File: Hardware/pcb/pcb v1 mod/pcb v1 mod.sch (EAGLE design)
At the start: 48 parts, among them K1 JS-M1-9V-4, K2 JS-M1-9V-4, Q1 32.768kHz 12.5pF, Q10 MOSFET-NCHANNELBSS138, Q3 MOSFET-NCHANNELBSS138, Q4 MOSFET-NCHANNELBSS138, Q5 MOSFET-NCHANNELBSS138, Q6 MOSFET-NCHANNELBSS138, Q7 MOSFET-NCHANNELBSS138, Q8 MOSFET-NCHANNELBSS138, Q9 MOSFET-NCHANNELBSS138, U1 ADP3338AKCZ-3.3RL7

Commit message: Ruteo completo
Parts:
- removed D1, D2: 1N5819HW, diego:1N5819HW
- removed D3: (no value), SparkFun-LED:WS2812B
- removed G1: BATTERY-HOLDER_11.6MM, battery:BATTERY-HOLDER_11.6MM
- removed K1, K2: JS-M1-9V-4, relay:JS-M1-9V-4
- removed Q10, Q3, Q4, Q5, Q6, Q7, Q8, Q9: MOSFET-NCHANNELBSS138, SparkFun-DiscreteSemi:MOSFET-NCHANNELBSS138
- removed R14, R16: 100, rcl:R-US_R0805
- removed R15, R17: 1M, rcl:R-US_R0805
- removed R18, R19: 10k, rcl:R-US_R0805
- removed RFID1: GROVE-RFID, partes:GROVE-RFID
- removed U$1: DS1307SO8, SparkFun-FreqCtrl:DS1307SO8
- removed X1, X2: (no value), con-wago-500:W237-103
- added C10, C9: 100nF, rcl:C-USC0805
- added C8: 22pF, rcl:C-USC1206
- added J1: AVR_SPI_PRG_6PTH, SparkFun-Connectors:AVR_SPI_PRG_6PTH
- added JP2, JP4, JP5: (no value), SparkFun-Connectors:M041X04_NO_SILK
- added JP3, JP7: (no value), SparkFun-Connectors:M03PTH
- added JP8, JP9: M02PTH, SparkFun-Connectors:M02PTH
- added LED1: 5MMRGBLED, adafruit:5MMRGBLED
- added LVLSHF1: LEVELSHIFTER4, partes:LEVELSHIFTER4
- added R3, R4: 10k, rcl:R-US_R0805
- added U2: ATMEGA328P, SparkFun-DigitalIC:ATMEGA328_SMT
- added Y1: 16Mhz, SparkFun-FreqCtrl:CRYSTALHC49US
- C1, C2: value 1uF -> 10uF; device rcl:CPOL-US150CLZ-1010 -> rcl:CPOL-USE2.5-6
- C3: device rcl:C-USC0805 -> rcl:C-USC1206
- C4: value 1uF -> 100nF
- C7: value 100nF -> 22pF; device rcl:C-USC0805 -> rcl:C-USC1206
- Q1: value 32.768kHz 12.5pF -> 2N3906; device crystal:CRYSTALTC26H -> transistor-pnp:2N3906
- R10: value 100 -> 160R; device rcl:R-US_R0805 -> rcl:R-US_R1206
- R11: value 1M -> 100R
- R12: value 100 -> 100R
- R13: value 1M -> 100K
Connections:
- removed net LED: Q10.S, R19.1
- removed net N$13: Q6.G, R10.2
- removed net N$24: Q9.D, SG1.2
- removed net N$26: D3.DIN, Q10.D, R18.1
- removed net RFIDPW: R10.1, R11.2
- removed net RFIDTX33: Q5.S, R8.1
- removed net SCL33: Q3.S, R5.1
- removed net SDA33: Q4.S, R7.1
- new net AT_RST: J1.5, R13.2, U2.PC6(/RESET)
- new net ESP_RX_33: JP8.1, LVLSHF1.LV2
- new net ESP_TX_33: JP9.1, LVLSHF1.LV1
- new net LED_B: R12.1, U2.PD6(AIN0)
- new net LED_G: R11.1, U2.PB2(SS/OC1B)
- new net LED_R: R10.1, U2.PB1(OC1A)
- new net N$10: LED1.RED, R10.2
- new net N$8: JP9.2, MDL1.TXD
- new net RFID_PW: R1.1, U2.PD5(T1)
- new net RFID_TX: JP4.4, U2.PD2(INT0)
- new net SCL: JP5.3, R7.1, U2.PC5(ADC5/SCL)
- new net SDA: JP5.4, R6.1, U2.PC4(ADC4/SDA)
- net +3V3: now also C10.1, C3.1, C4.1, JP3.3, LVLSHF1.LV, MDL1.VCC, R4.2, R9.2; no longer C7.1, Q10.G, Q3.G, Q4.G, Q5.G, R19.2, R5.2, R7.2
- net +5V: now also C9.1, J1.2, JP2.4, JP5.2, LVLSHF1.HV, Q1.E, R13.1, R7.2, U2.AVCC, U2.VCC@1, U2.VCC@2; no longer C3.1, C4.1, C6.1, D1.C, D2.C, D3.VDD, K11.1, K21.1, R1.2, R18.2, R9.2, RFID1.VCC, SG1.1, U$1.VCC
- net BUZZER: now also SG1.1, U2.PC0(ADC0); no longer R16.1, R17.2
- net GND: now also C10.2, C8.2, C9.2, J1.6, JP2.1, JP3.1, JP4.1, JP5.1, JP7.2, LED1.GND, LVLSHF1.GND, MDL1.GND, R3.1, SG1.2, U2.AGND, U2.GND@1, U2.GND@2; no longer D3.VSS, G1.-, Q6.S, Q7.S, Q8.S, Q9.S, R11.1, R13.1, R15.1, R17.1, U$1.GND
- net N$11: now also C7.1, U2.PB6(XTAL1/TOSC1), Y1.1; no longer Q5.D, R9.1, RFID1.TX
- net N$12: now also C8.1, U2.PB7(XTAL2/TOSC2), Y1.2; no longer D1.A, K11.2, Q7.D
- net N$14: now also C6.1, U2.AREF; no longer Q7.G, R12.2
- net N$15: now also LED1.GREEN, R11.2; no longer K12.O, X1-3.KL
- net N$16: now also LED1.BLUE, R12.2; no longer K12.P, X1-2.KL
- net N$17: now also J1.3, U2.PB5(SCK); no longer K12.S, X1-1.KL
- net N$18: now also J1.1, U2.PB4(MISO); no longer D2.A, K21.2, Q8.D
- net N$19: now also J1.4, U2.PB3(MOSI/OC2); no longer Q8.G, R14.2
- net N$2: now also MDL1.CH_PD, R8.1; no longer Q1.2, U$1.X1
- net N$20: now also JP3.2, R5.2; no longer K22.O, X2-3.KL
- net N$21: now also LVLSHF1.HV1, U2.PD0(RXD); no longer K22.P, X2-2.KL
- net N$22: now also LVLSHF1.HV2, U2.PD1(TXD); no longer K22.S, X2-1.KL
- net N$23: now also JP4.2, Q1.C; no longer Q9.G, R16.2
- net N$3: now also MDL1.GPIO2, R4.1; no longer Q1.1, U$1.X2
- net N$4: now also MDL1.GPIO0, R5.1; no longer G1.+, U$1.VBATT
- net N$5: now also MDL1.GPIO15, R3.2; no longer Q3.D, R2.1, U$1.SCL
- net N$6: now also JP8.2, MDL1.RXD; no longer R1.1, U$1.SQW
- net N$7: now also Q1.B, R1.2, R2.1; no longer Q6.D, RFID1.GND
- net N$9: now also JP7.1, MDL1.REST, R9.1; no longer Q4.D, R6.1, U$1.SDA
- net RELE1: now also JP2.3, U2.PC1(ADC1); no longer R12.1, R13.2
- net RELE2: now also JP2.2, U2.PC2(ADC2); no longer R14.1, R15.2
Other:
- moved on the sheet: C1, C2, C3, C4, C5, C6, C7, JP1, MDL1, R1, R10, R11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

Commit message: Correcciones placa
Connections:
- net GND: now also JP1.2; no longer JP1.1
- net N$1: now also JP1.1; no longer JP1.2
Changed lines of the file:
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@@
 <wire x1="259.08" y1="27.94" x2="259.08" y2="20.32" width="0.1524" layer="91"/>
 <junction x="259.08" y="20.32"/>
-<pinref part="JP1" gate="G$1" pin="1"/>
-<wire x1="228.6" y1="30.48" x2="231.14" y2="30.48" width="0.1524" layer="91"/>
-<wire x1="231.14" y1="30.48" x2="231.14" y2="20.32" width="0.1524" layer="91"/>
+<wire x1="231.14" y1="33.02" x2="231.14" y2="20.32" width="0.1524" layer="91"/>
 <wire x1="231.14" y1="20.32" x2="251.46" y2="20.32" width="0.1524" layer="91"/>
 <junction x="251.46" y="20.32"/>
 <pinref part="C1" gate="G$1" pin="-"/>
+<pinref part="JP1" gate="G$1" pin="2"/>
+<wire x1="228.6" y1="33.02" x2="231.14" y2="33.02" width="0.1524" layer="91"/>
 </segment>
 <segment>
@@
 </segment>
 </net>
-<net name="N$1" class="0">
-<segment>
-<pinref part="JP1" gate="G$1" pin="2"/>
-<pinref part="S1" gate="1" pin="P"/>
-<wire x1="228.6" y1="33.02" x2="236.22" y2="33.02" width="0.1524" layer="91"/>
-</segment>
-</net>
 <net name="RFID_PW" class="0">
 <segment>
@@
 </segment>
 </net>
+<net name="N$1" class="0">
+<segment>
+<pinref part="JP1" gate="G$1" pin="1"/>
+<wire x1="228.6" y1="30.48" x2="233.68" y2="30.48" width="0.1524" layer="91"/>
+<wire x1="233.68" y1="30.48" x2="233.68" y2="33.02" width="0.1524" layer="91"/>
+<pinref part="S1" gate="1" pin="P"/>
+<wire x1="233.68" y1="33.02" x2="236.22" y2="33.02" width="0.1524" layer="91"/>
+</segment>
+</net>

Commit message: Cambios menores
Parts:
- JP8: value M02PTH -> (none); device SparkFun-Connectors:M02PTH -> SparkFun-Connectors:M03PTH
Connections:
- net GND: now also JP8.3
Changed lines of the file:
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@@
 <part name="GND16" library="supply1" deviceset="GND" device=""/>
 <part name="LED1" library="adafruit" deviceset="5MMRGBLED" device=""/>
-<part name="JP8" library="SparkFun-Connectors" deviceset="M02" device="PTH"/>
+<part name="JP8" library="SparkFun-Connectors" deviceset="M03" device="PTH"/>
 <part name="JP9" library="SparkFun-Connectors" deviceset="M02" device="PTH"/>
 <part name="JP4" library="SparkFun-Connectors" deviceset="M04" device="1X04_NO_SILK"/>
@@
 <instance part="GND16" gate="1" x="187.96" y="73.66"/>
 <instance part="LED1" gate="G$1" x="309.88" y="160.02"/>
-<instance part="JP8" gate="G$1" x="35.56" y="114.3" rot="R90"/>
+<instance part="JP8" gate="G$1" x="33.02" y="114.3" rot="R90"/>
 <instance part="JP9" gate="G$1" x="50.8" y="114.3" rot="R90"/>
 <instance part="JP4" gate="G$1" x="299.72" y="71.12" rot="MR0"/>
@@
 <junction x="22.86" y="144.78"/>
 <pinref part="JP3" gate="G$1" pin="1"/>
-</segment>
-<segment>
+<pinref part="JP8" gate="G$1" pin="3"/>
+<wire x1="27.94" y1="132.08" x2="30.48" y2="132.08" width="0.1524" layer="91"/>
+<wire x1="30.48" y1="132.08" x2="30.48" y2="121.92" width="0.1524" layer="91"/>
+<junction x="27.94" y="132.08"/>
+</segment>
+<segment>

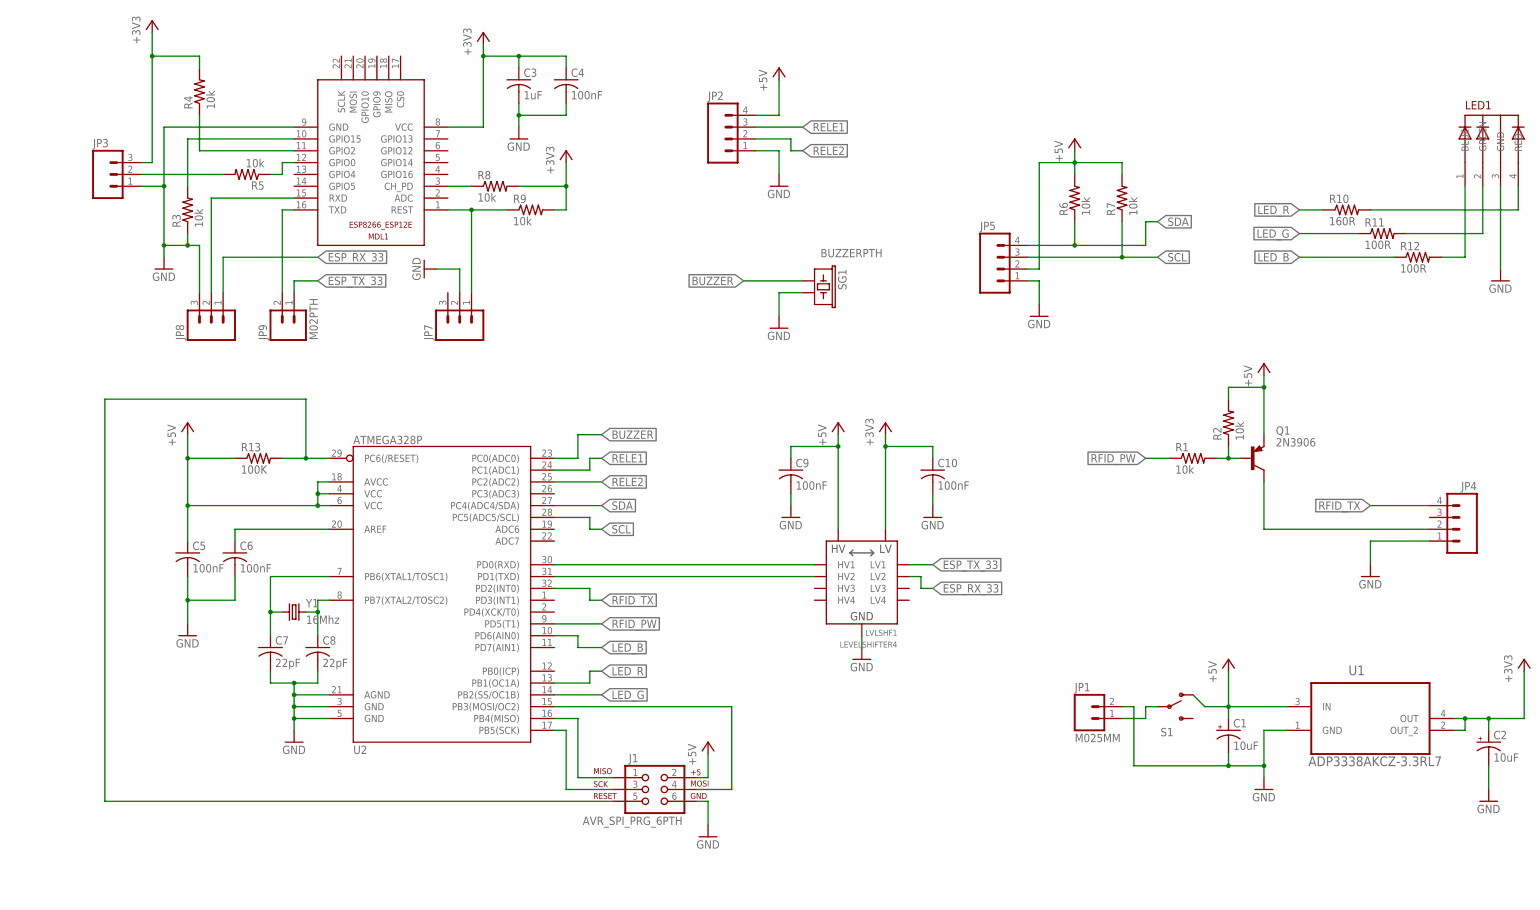
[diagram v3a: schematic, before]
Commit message: Cambio de valores de condensadores
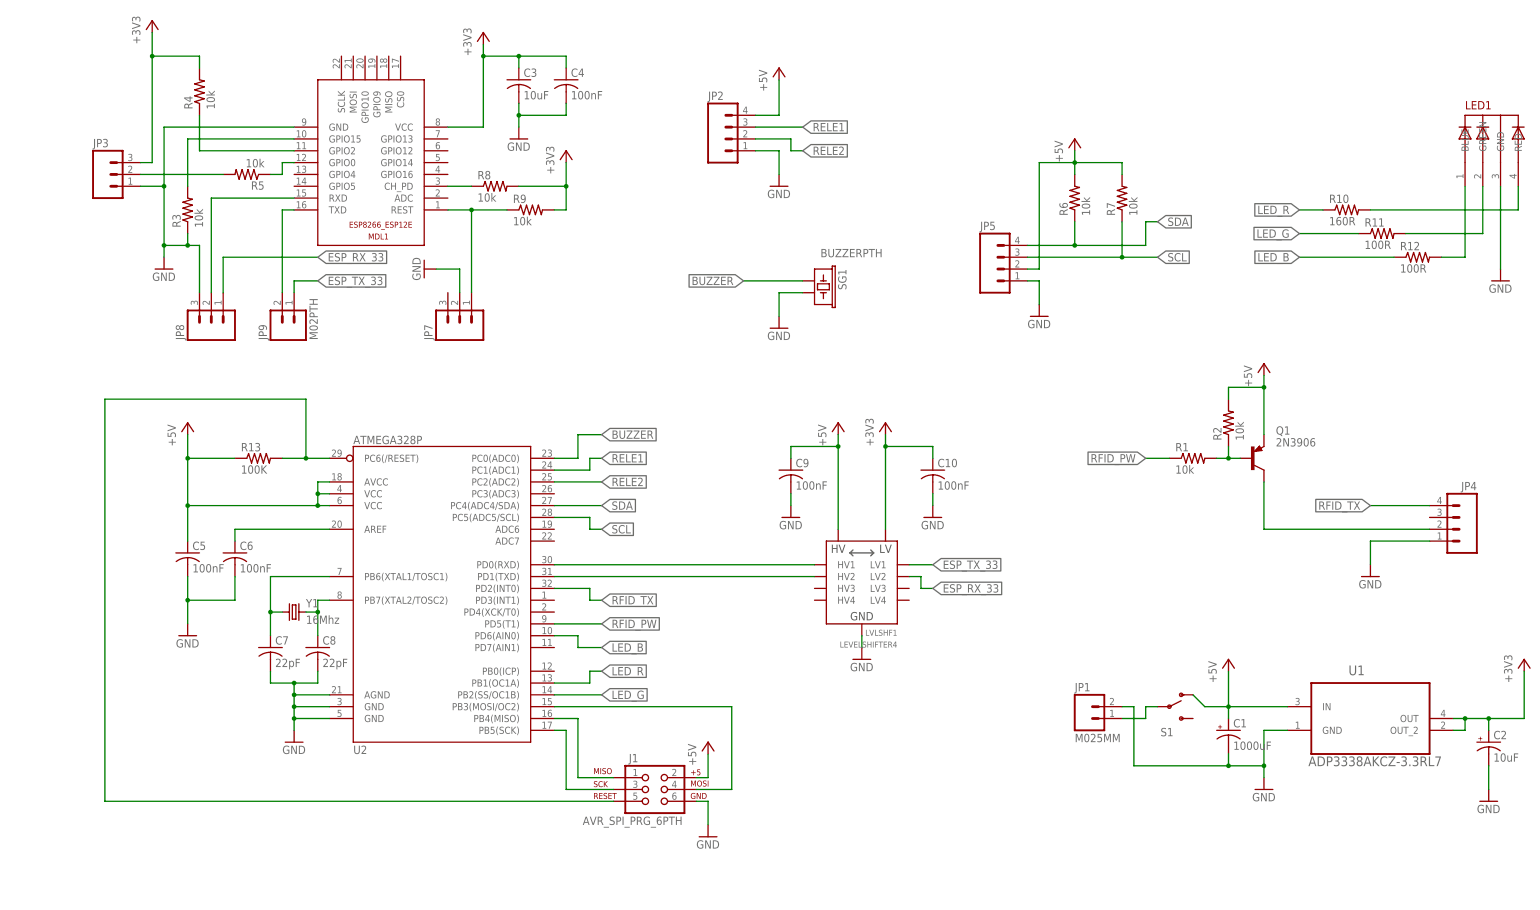
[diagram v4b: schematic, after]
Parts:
- C1: value 10uF -> 1000uF
- C3: value 1uF -> 10uF
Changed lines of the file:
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@@
 <?xml version="1.0" encoding="utf-8"?>
 <!DOCTYPE eagle SYSTEM "eagle.dtd">
-<eagle version="7.4.0">
+<eagle version="7.3.0">
 <drawing>
 <settings>
@@
 <part name="R12" library="rcl" deviceset="R-US_" device="R0805" value="100R"/>
 <part name="GND10" library="supply1" deviceset="GND" device=""/>
-<part name="C3" library="rcl" deviceset="C-US" device="C1206" value="1uF"/>
+<part name="C3" library="rcl" deviceset="C-US" device="C1206" value="10uF"/>
 <part name="C4" library="rcl" deviceset="C-US" device="C0805" value="100nF"/>
 <part name="GND9" library="supply1" deviceset="GND" device=""/>
@@
 <part name="Q1" library="transistor-pnp" deviceset="2N3906" device=""/>
 <part name="R1" library="rcl" deviceset="R-US_" device="R0805" value="10k"/>
-<part name="C1" library="rcl" deviceset="CPOL-US" device="E2.5-6" value="10uF"/>
+<part name="C1" library="rcl" deviceset="CPOL-US" device="E2.5-6" value="1000uF"/>
 <part name="C2" library="rcl" deviceset="CPOL-US" device="E2.5-6" value="10uF"/>
 <part name="C10" library="rcl" deviceset="C-US" device="C0805" value="100nF"/>

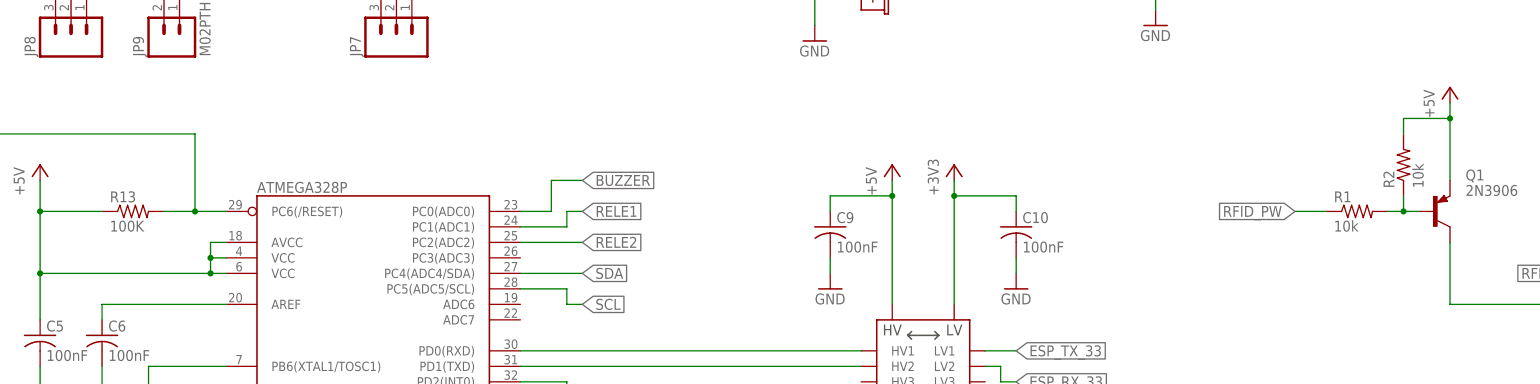
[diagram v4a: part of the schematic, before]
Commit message: Cambios en algunas resistencias
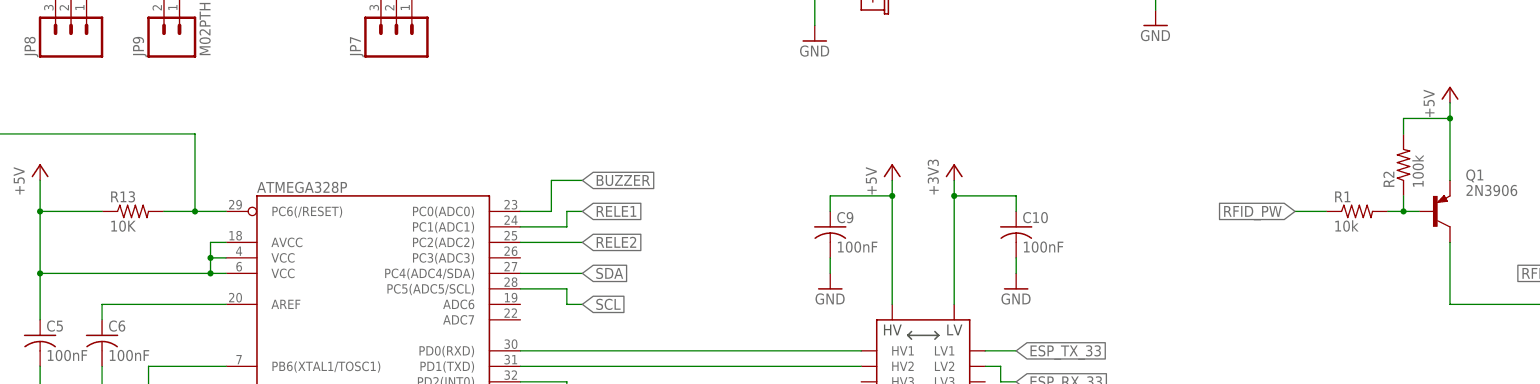
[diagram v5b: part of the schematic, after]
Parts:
- R13: value 100K -> 10K
- R2: value 10k -> 100k
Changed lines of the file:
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@@
 <part name="C8" library="rcl" deviceset="C-US" device="C1206" value="22pF"/>
 <part name="GND12" library="supply1" deviceset="GND" device=""/>
-<part name="R13" library="rcl" deviceset="R-US_" device="R0805" value="100K"/>
+<part name="R13" library="rcl" deviceset="R-US_" device="R0805" value="10K"/>
 <part name="J1" library="SparkFun-Connectors" deviceset="AVR_SPI_PRG_6" device="PTH"/>
 <part name="GND13" library="supply1" deviceset="GND" device=""/>
@@
 <part name="GND15" library="supply1" deviceset="GND" device=""/>
 <part name="LVLSHF1" library="partes" deviceset="LEVELSHIFTER4" device=""/>
-<part name="R2" library="rcl" deviceset="R-US_" device="R0805" value="10k"/>
+<part name="R2" library="rcl" deviceset="R-US_" device="R0805" value="100k"/>
 <part name="Q1" library="transistor-pnp" deviceset="2N3906" device=""/>
 <part name="R1" library="rcl" deviceset="R-US_" device="R0805" value="10k"/>
